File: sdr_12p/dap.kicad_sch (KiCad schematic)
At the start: 32 parts, among them U1 SI53301-B-GM, U2 ADAU1467WBCPZ300

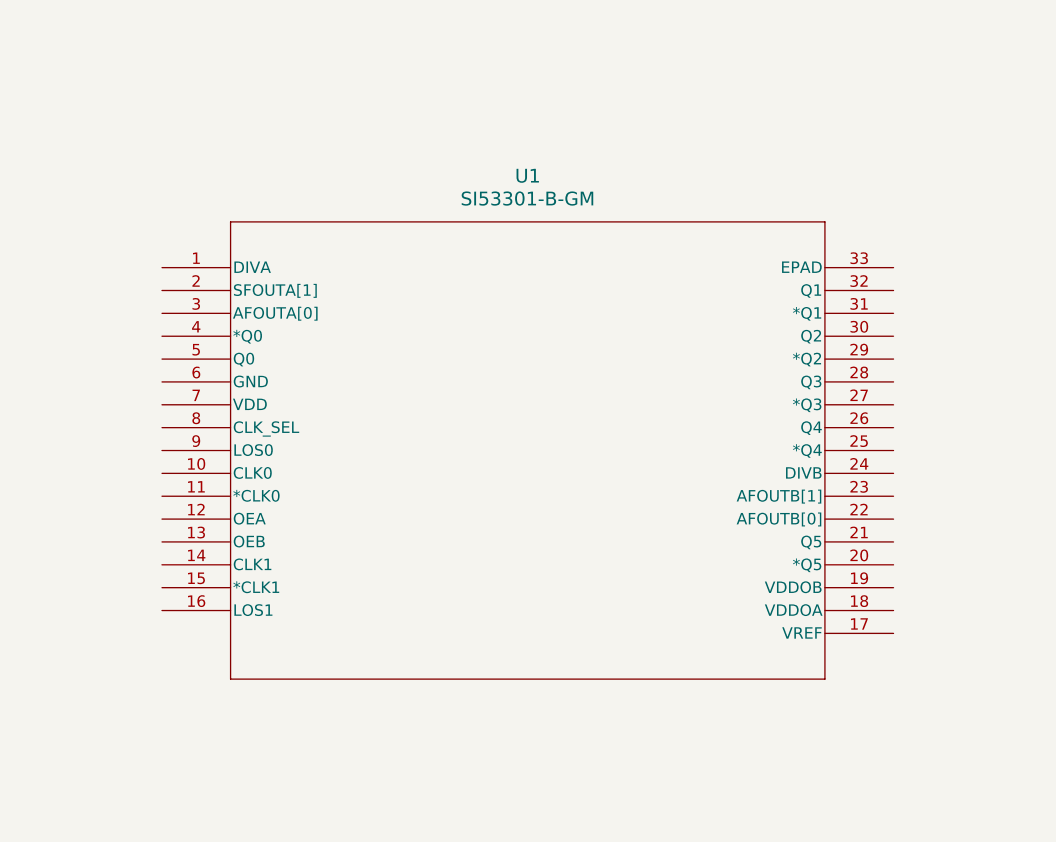
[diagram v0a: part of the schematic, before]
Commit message: added uC
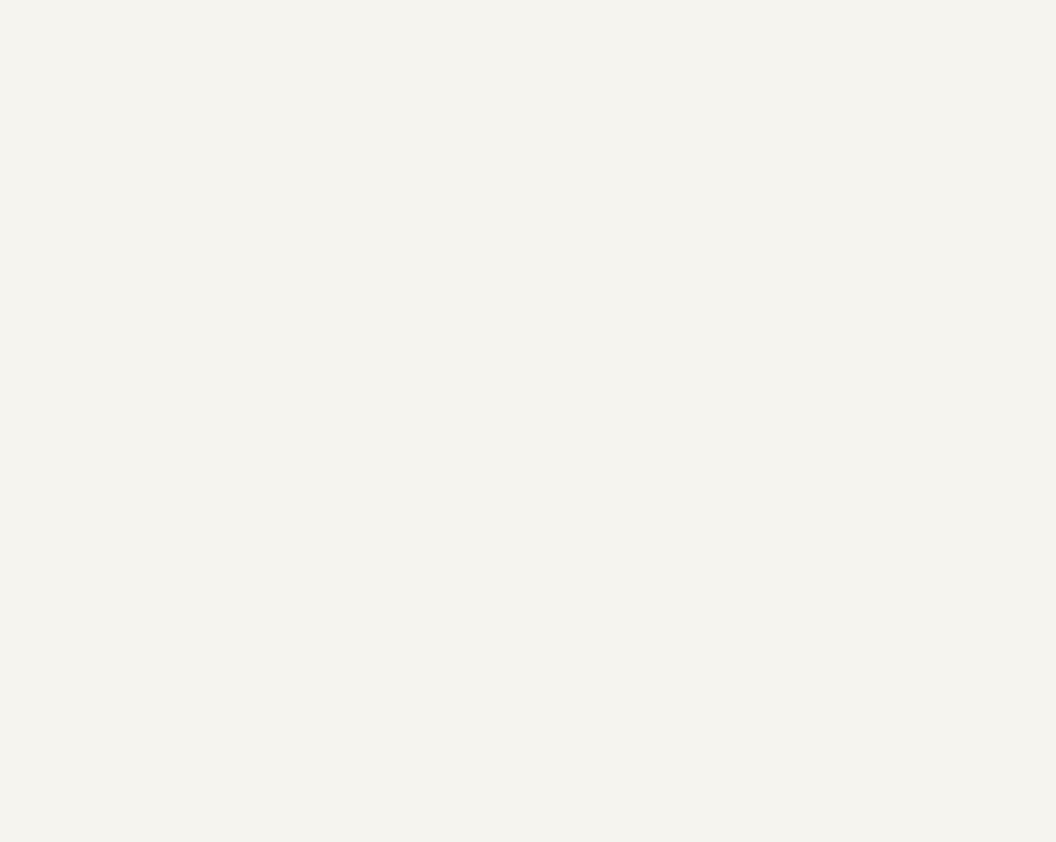
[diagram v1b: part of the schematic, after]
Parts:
- removed U1: SI53301-B-GM, QFN32_5X5_SIL, symbol Si53301:SI53301-B-GM
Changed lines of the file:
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@@
-	)
-	(symbol
-		(lib_id "Si53301:SI53301-B-GM")
-		(at 290.83 165.1 0)
-		(unit 1)
-		(exclude_from_sim no)
-		(in_bom yes)
-		(on_board yes)
-		(dnp no)
-		(fields_autoplaced yes)
-		(property "Reference" "U1"
-			(at 331.47 154.94 0)
-			(effects
-				(font
-					(size 1.524 1.524)
-				)
-			)
-		)
-		(property "Value" "SI53301-B-GM"
-			(at 331.47 157.48 0)
-			(effects
-				(font
-					(size 1.524 1.524)
-				)
-			)
-		)
-		(property "Footprint" "QFN32_5X5_SIL"
-			(at 290.83 165.1 0)
-			(effects
-				(font
-					(size 1.27 1.27)
-					(italic yes)
-				)
-				(hide yes)
-			)
-		)
-		(property "Datasheet" "SI53301-B-GM"
-			(at 290.83 165.1 0)
-			(effects
-				(font
-					(size 1.27 1.27)
-					(italic yes)
-				)
-				(hide yes)
-			)
-		)
-		(property "Description" ""
-			(at 290.83 165.1 0)
-			(effects
-				(font
-					(size 1.27 1.27)
-				)
-				(hide yes)
-			)
-		)
-		(pin "21"
-		)
-		(pin "7"
-		)
-		(pin "25"
-		)
-		(pin "16"
-		)
-		(pin "32"
-		)
-		(pin "17"
-		)
-		(pin "30"
-		)
-		(pin "3"
-		)
-		(pin "28"
-		)
-		(pin "26"
-		)
-		(pin "29"
-		)
-		(pin "15"
-		)
-		(pin "23"
-		)
-		(pin "10"
-		)
-		(pin "22"
-		)
-		(pin "20"
-		)
-		(pin "24"
-		)
-		(pin "2"
-		)
-		(pin "1"
-		)
-		(pin "31"
-		)
-		(pin "27"
-		)
-		(pin "13"
-		)
-		(pin "18"
-		)
-		(pin "5"
-		)
-		(pin "4"
-		)
-		(pin "33"
-		)
-		(pin "14"
-		)
-		(pin "9"
-		)
-		(pin "19"
-		)
-		(pin "11"
-		)
-		(pin "12"
-		)
-		(pin "8"
-		)
-		(pin "6"
-		)
-		(instances
-			(project "sdr_12p"
-				(path "/fe42ca2f-2bb8-4d5a-9e84-807788ed632f/fa60d9db-5fbc-4f32-9a00-e3130bb41db9"
-					(reference "U1")
-					(unit 1)
-				)
-			)
-		)
 	)
 	(symbol
